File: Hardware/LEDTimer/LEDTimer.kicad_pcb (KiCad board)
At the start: 2 copper layers, 22 parts, among them J1 ICSP, J2 LED, J3 PWR_IN, SW1 SW_Push, SW2 SW_Push, SW3 SW_Push, U1 AP7383-36WW7, U2 PIC16F1825, U3 Display_128x64_096_I2C, U4 BCR_421U_E6327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

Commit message: PCB: add footprint libraries
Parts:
- removed Rext1: R, Resistor_SMD:R_0805_2012Metric_Pad1.20x1.40mm_HandSolder
- added BT1: HU2032-LF, Renata HU2032LF:Renata-HU2032-LF-0-0-0, B.Cu at (67.6, 47.8)
- added R4: 4k7, Resistor_SMD:R_0805_2012Metric_Pad1.20x1.40mm_HandSolder, F.Cu at (66.4, 37.9)
- added R6: 4k7, Resistor_SMD:R_0805_2012Metric_Pad1.20x1.40mm_HandSolder, F.Cu at (70.3, 37.9)
- added RVext1: R_Potentiometer, Potentiometer_SMD:Potentiometer_Vishay_TS53YJ_Vertical, F.Cu at (135.2, 113.8)
- added SW4: SW_SPDT, SPDT Switch:1825232-1, F.Cu at (80.2, 40.9)
- R1: value 24k -> 47k
- Y1: value 32.768kHz -> 32.768 kHz; footprint Crystal:Crystal_AT310_D3.0mm_L10.0mm_Horizontal_1EP_style2 -> Crystal:Crystal_SMD_Abracon_ABS25-4Pin_8.0x3.8mm
- moved J1 110.3 mm to (54.4, 59.9), turned to 90 degrees
- moved U3 74.3 mm to (67.5, 40.9)
- moved D1 69.6 mm to (92.1, 53.8), turned to 180 degrees
- moved CG1 56.6 mm to (191.5, 84.5), turned to -90 degrees
- moved Y1 47.4 mm to (195.6, 86.2)
- moved RD1 41.9 mm to (199.7, 83.6), turned to -90 degrees
- moved U2 29.6 mm to (197.9, 77.3), turned to 90 degrees
- moved CD1 24.4 mm to (199.7, 87.4), turned to -90 degrees
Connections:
- D1 pad 1: /VBAT_SENSE -> Net-(D1-Pad1)
- U2 pad 8: /VBAT_SENSE -> unconnected-(U2-Pad8)
- Y1 pad 2: Net-(CD1-Pad1) -> GND
- Y1 pad 3: (no net) -> GND
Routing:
- net Net-(CG1-Pad1): track 0.00 -> 6.80 mm
- net Net-(RD1-Pad1): track 0.00 -> 4.93 mm
- net Net-(CD1-Pad1): track 0.00 -> 4.78 mm
- added copper zone on B.Cu, net GND
- added copper zone on F.Cu, net GND
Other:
- board outline added: 68.8 x 56.3 mm

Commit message: PCB: start laying out the board
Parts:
- removed R5: 1k, Resistor_SMD:R_0805_2012Metric_Pad1.20x1.40mm_HandSolder
- RVext1, U4: moved to B.Cu
- SW1, SW2, SW3: footprint Button_Switch_SMD:SW_Push_1P1T_NO_6x6mm_H9.5mm -> LEDTimer:EVQ9P701P
- moved CD1 146.3 mm to (58.3, 50.1), turned to 180 degrees
- moved Y1 141.9 mm to (59.5, 46.0), turned to -90 degrees
- moved RD1 141.6 mm to (62.2, 50.1), turned to 180 degrees
- moved CG1 138.7 mm to (59.5, 41.8), turned to 180 degrees
- moved U2 131.6 mm to (69.4, 49.1), turned to 0 degrees
- moved J3 104.9 mm to (63.5, 58.3), turned to 180 degrees
- moved SW2 104.1 mm to (67.5, 65.1), turned to 180 degrees
- moved SW1 103.8 mm to (56.8, 65.1), turned to 180 degrees
- moved R1 100.5 mm to (76.5, 48.1), turned to 180 degrees
- moved R3 99.7 mm to (67.5, 43.5)
- moved U1 95.9 mm to (67.1, 57.2), turned to 90 degrees
- moved C2 93.3 mm to (76.6, 52.2), turned to 180 degrees
- moved R2 89.7 mm to (76.5, 50.1)
- moved C1 88.7 mm to (67.3, 60.4)
- moved SW3 84.0 mm to (78.2, 65.1), turned to 180 degrees
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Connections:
- D1 pad 1: Net-(D1-Pad1) -> Net-(C2-Pad1)
- D1 pad 2: Net-(C2-Pad1) -> Net-(D1-Pad2)
- SW1 pad 1: /ICSPDAT -> GND
- SW1 pad 2: GND -> /ICSPDAT
- SW2 pad 1: /ICSPCLK -> GND
- SW2 pad 2: GND -> /ICSPCLK
- SW4 pad 1: Net-(D1-Pad1) -> Net-(BT1-Pad2)
- SW4 pad 2: Net-(BT1-Pad2) -> Net-(D1-Pad2)
- U4 pad 1: Net-(R5-Pad2) -> /LED_EN_PWM
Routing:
- net Net-(SW3-Pad2): track 0.00 -> 24.3 mm
- net Net-(C2-Pad1): track 0.00 -> 19.9 mm, vias 0 -> 3
- net +3V3: track 0.00 -> 16.3 mm, vias 0 -> 2
- net Net-(R4-Pad2): track 0.00 -> 12.3 mm, vias 0 -> 2
- net Net-(R6-Pad2): track 0.00 -> 12.1 mm
- net GND: track 0.00 -> 11.0 mm, vias 0 -> 6
- net Net-(J2-Pad2): track 0.00 -> 10.8 mm
- net Net-(BT1-Pad2): track 0.00 -> 8.59 mm
- net Net-(RVext1-Pad1): track 0.00 -> 8.15 mm
- net /~{MCLR}/VPP: track 0.00 -> 7.34 mm
- net /LDO_SENSE: track 0.00 -> 5.62 mm
- net +5V: track 0.00 -> 4.80 mm
- net /ICSPDAT: track 0.00 -> 3.85 mm
- net /ICSPCLK: track 0.00 -> 3.85 mm
- net Net-(D1-Pad2): track 0.00 -> 3.82 mm
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
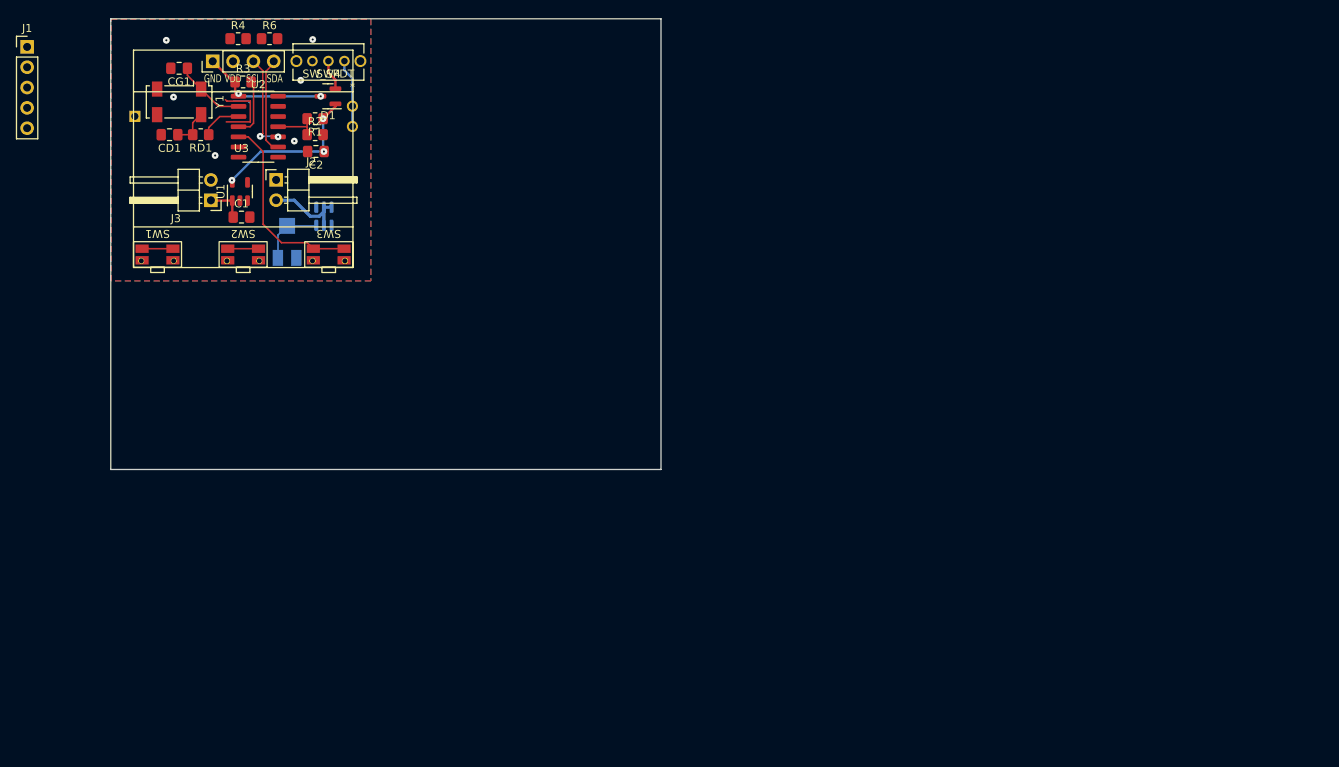
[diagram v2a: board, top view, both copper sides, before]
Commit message: PCB: first version of the layout
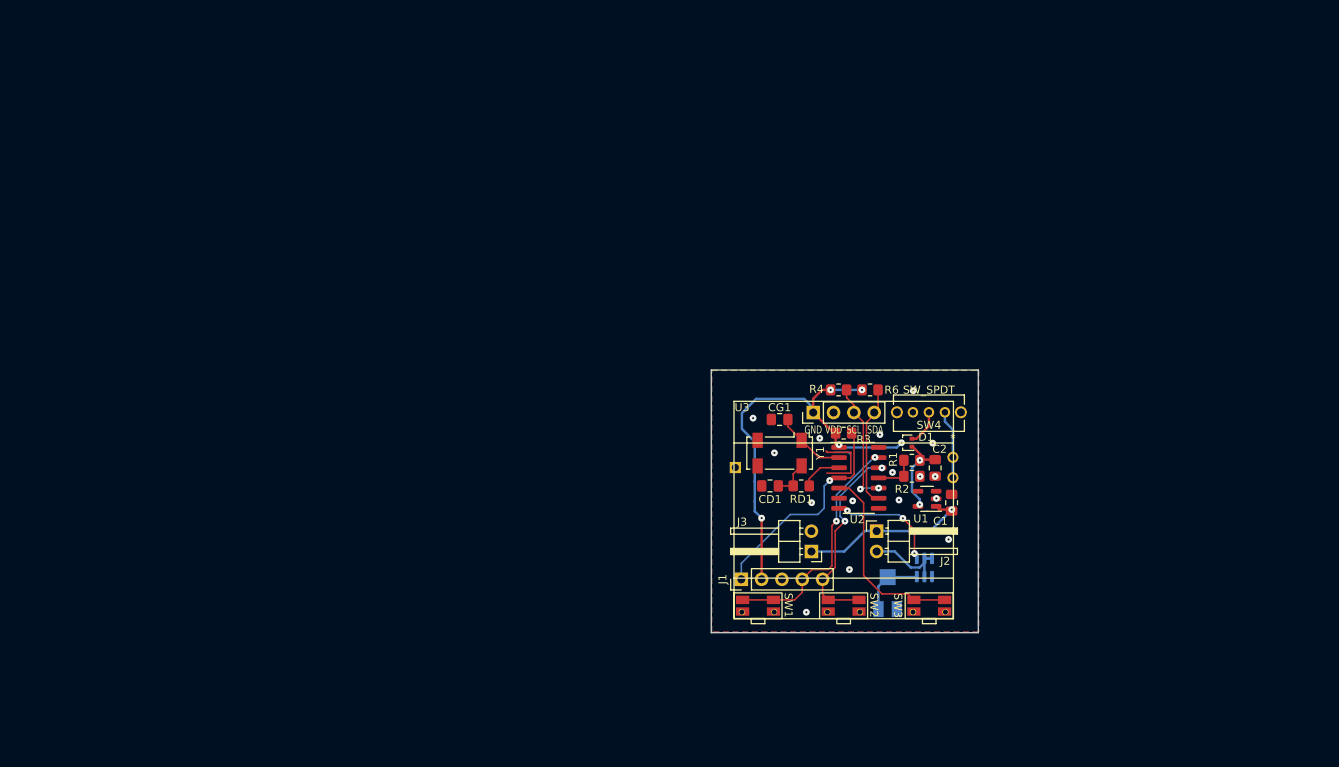
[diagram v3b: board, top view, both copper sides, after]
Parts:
- D1: footprint Package_TO_SOT_SMD:SOT-23 -> Package_TO_SOT_SMD:SOT-416
- moved J1 111.3 mm to (129.8, 105.7), turned to 90 degrees
- moved C1 95.7 mm to (156.1, 96.1), turned to 90 degrees
- moved U1 94.1 mm to (153.0, 95.6), turned to 180 degrees
- moved BT1 87.0 mm to (142.6, 91.7)
- moved CG1 87.0 mm to (134.6, 85.7)
- moved J2 87.0 mm to (146.7, 99.7)
- moved J3 87.0 mm to (138.5, 102.2)
- moved R3 87.0 mm to (142.6, 87.4)
- moved R4 87.0 mm to (141.9, 82.0)
- moved RVext1 87.0 mm to (148.1, 107.4)
- moved SW2 87.0 mm to (142.6, 109.0)
- moved U4 87.0 mm to (152.7, 104.2)
- moved Y1 87.0 mm to (134.6, 89.9)
- moved CD1 87.0 mm to (133.4, 94.0)
- moved R6 87.0 mm to (145.9, 82.0)
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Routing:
- net +3V3: track 16.3 -> 54.8 mm, vias 2 -> 5
- net /ICSPDAT: track 3.85 -> 29.8 mm, vias 0 -> 2
- net /ICSPCLK: track 3.85 -> 25.3 mm, vias 0 -> 2
- net /~{MCLR}/VPP: track 7.34 -> 27.6 mm, vias 0 -> 1
- net +5V: track 4.80 -> 21.9 mm, vias 0 -> 1
- net /LED_EN_PWM: track 0.00 -> 14.2 mm, vias 0 -> 3
- net Net-(C2-Pad1): track 19.9 -> 10.8 mm, vias 3 -> 2
- net Net-(R4-Pad2): track 12.3 -> 15.8 mm
- net Net-(R6-Pad2): track 12.1 -> 15.2 mm
- net Net-(D1-Pad2): track 3.82 -> 4.52 mm
- net GND: vias 6 -> 16
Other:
- board size 68.8 x 56.3 mm -> 33.4 x 32.8 mm
- board text removed: "3.3V"
- board text removed: "MCLR"

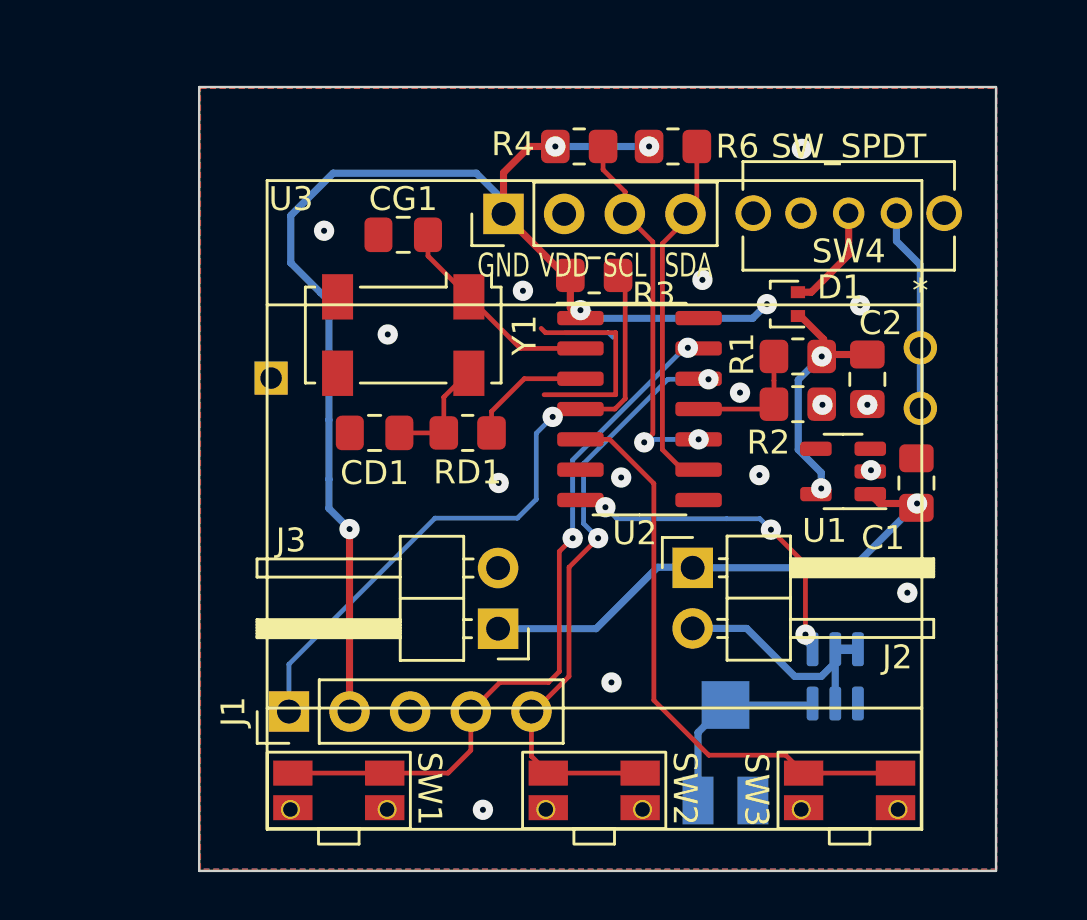
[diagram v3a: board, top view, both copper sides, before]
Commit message: PCB: new layout (not routed yet)
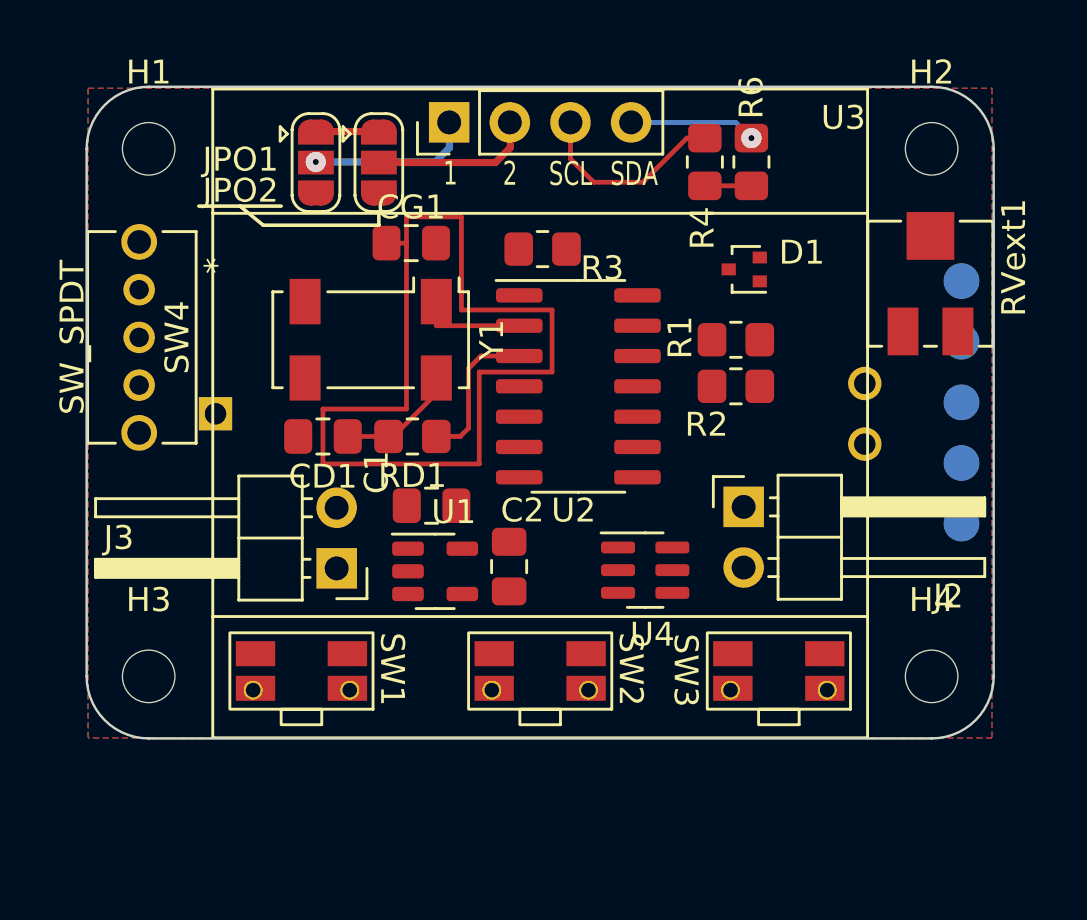
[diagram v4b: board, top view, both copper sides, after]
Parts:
- removed J1: ICSP, Connector_PinHeader_2.54mm:PinHeader_1x05_P2.54mm_Vertical
- added H1: MountingHole, MountingHole:MountingHole_2.2mm_M2, F.Cu at (123.9, 82.1)
- added H2: MountingHole, MountingHole:MountingHole_2.2mm_M2, F.Cu at (156.7, 82.1)
- added H3: MountingHole, MountingHole:MountingHole_2.2mm_M2, F.Cu at (123.9, 104.2)
- added H4: MountingHole, MountingHole:MountingHole_2.2mm_M2, F.Cu at (156.7, 104.2)
- added JPO1: OLED1, Jumper:SolderJumper-3_P1.3mm_Open_RoundedPad1.0x1.5mm, F.Cu at (130.9, 82.7)
- added JPO2: OLED2, Jumper:SolderJumper-3_P1.3mm_Open_RoundedPad1.0x1.5mm, F.Cu at (133.5, 82.7)
- added TP1: ~{MCLR}/VPP, TestPoint:TestPoint_Pad_D1.5mm, B.Cu at (157.9, 87.6)
- added TP2: +3V3, TestPoint:TestPoint_Pad_D1.5mm, B.Cu at (157.9, 90.2)
- added TP3: GND, TestPoint:TestPoint_Pad_D1.5mm, B.Cu at (157.9, 92.7)
- added TP4: ICSPDAT, TestPoint:TestPoint_Pad_D1.5mm, B.Cu at (157.9, 95.3)
- added TP5: ICSPCLK, TestPoint:TestPoint_Pad_D1.5mm, B.Cu at (157.9, 97.8)
- RVext1, U4: moved to F.Cu
- moved SW4 31.9 mm to (123.5, 88.0), turned to -90 degrees
- moved RVext1 21.4 mm to (156.7, 87.8)
- moved C1 20.3 mm to (135.8, 97.0), turned to 0 degrees
- moved U1 17.6 mm to (135.9, 99.8), turned to 0 degrees
- moved C2 16.9 mm to (139.0, 99.6)
- moved U4 9.12 mm to (144.7, 99.8), turned to 0 degrees
- moved J3 7.22 mm to (131.8, 99.7)
- moved SW3 5.81 mm to (150.3, 104.0)
- moved SW2 5.49 mm to (140.3, 104.0)
- moved R4 5.30 mm to (147.2, 82.7), turned to 90 degrees
- moved SW1 5.24 mm to (130.3, 104.0)
- moved U3 4.46 mm to (140.3, 81.0)
- moved R6 3.35 mm to (149.2, 82.7), turned to 90 degrees
- moved J2 3.33 mm to (148.8, 97.1)
- moved BT1 2.77 mm to (140.3, 93.2)
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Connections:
- U3 pad 1: +3V3 -> /OLED1
- U3 pad 2: GND -> /OLED2
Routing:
- net +3V3: track 54.8 -> 4.59 mm, vias 5 -> 0
- net /ICSPDAT: track 29.8 -> 0.00 mm, vias 2 -> 0
- net /~{MCLR}/VPP: track 27.6 -> 0.00 mm, vias 1 -> 0
- net /ICSPCLK: track 25.3 -> 0.00 mm, vias 2 -> 0
- net Net-(SW3-Pad2): track 24.3 -> 0.00 mm
- net +5V: track 21.9 -> 0.00 mm, vias 1 -> 0
- net /LED_EN_PWM: track 14.2 -> 0.00 mm, vias 3 -> 0
- net GND: track 11.0 -> 0.00 mm, vias 16 -> 0
- net Net-(C2-Pad1): track 10.8 -> 0.00 mm, vias 2 -> 0
- net Net-(J2-Pad2): track 10.8 -> 0.00 mm
- net Net-(R6-Pad2): track 15.2 -> 5.31 mm, vias 0 -> 1
- net Net-(BT1-Pad2): track 8.59 -> 0.00 mm
- net Net-(RVext1-Pad1): track 8.15 -> 0.00 mm
- net Net-(R4-Pad2): track 15.8 -> 8.33 mm, vias 2 -> 0
- net /OLED1: track 0.00 -> 6.91 mm, vias 0 -> 1
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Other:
- board size 33.4 x 32.8 mm -> 38 x 27.3 mm
